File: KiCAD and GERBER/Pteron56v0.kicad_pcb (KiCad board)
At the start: 2 copper layers, 136.1 x 108.1 mm, 46 parts, among them J1 AudioJack4, J2 AudioJack4, SW10 SW_PUSH, SW12 SW_PUSH, SW13 SW_PUSH, SW14 SW_PUSH, SW15 SW_PUSH, SW17 SW_PUSH, SW18 SW_PUSH, SW19 SW_PUSH, SW20 SW_PUSH, SW22 SW_PUSH, SW23 SW_PUSH, SW24 SW_PUSH, SW26 SW_PUSH, SW27 SW_PUSH, SW28 SW_PUSH, SW7 SW_PUSH, SW8 SW_PUSH, SW9 SW_PUSH, U1 ProMicro

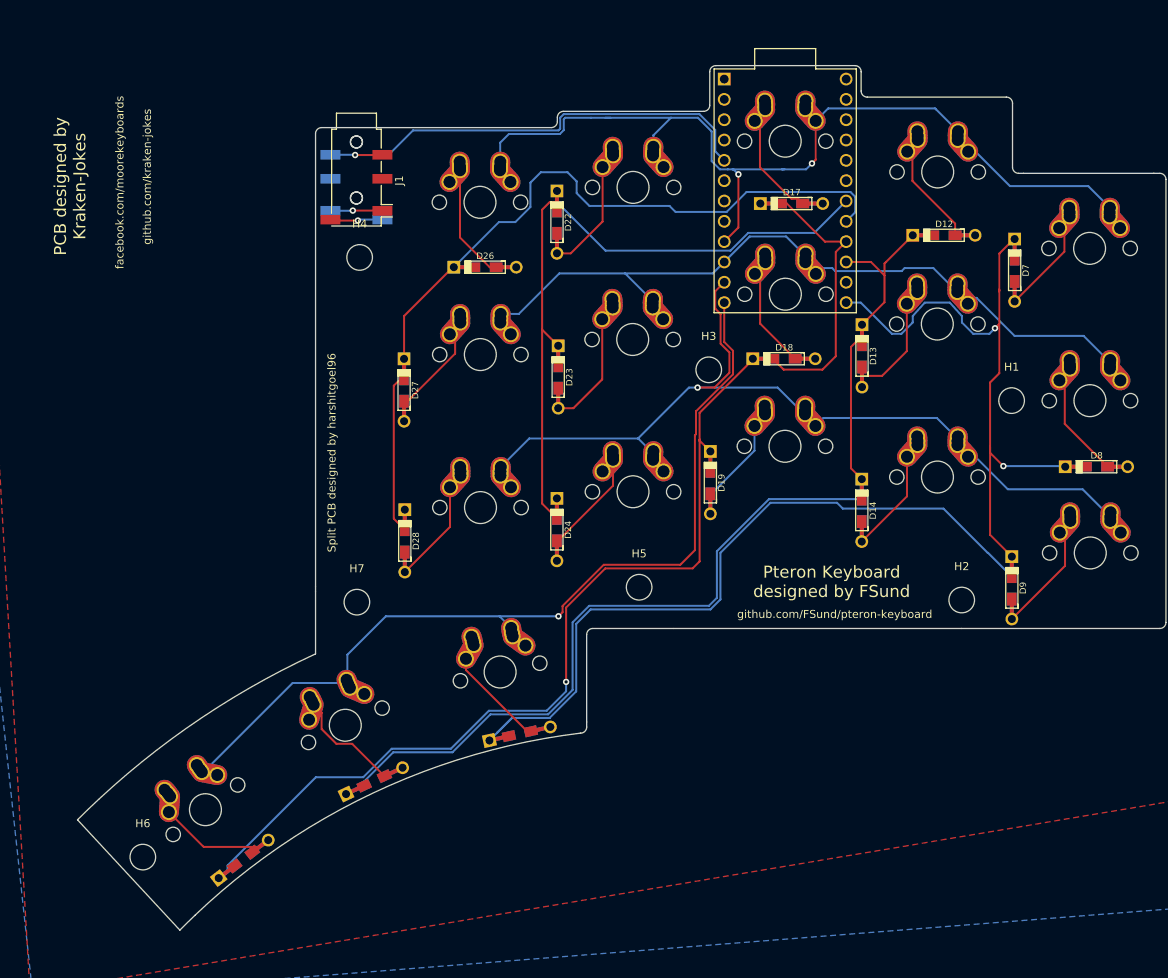
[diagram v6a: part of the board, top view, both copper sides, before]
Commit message: simplified wiring, lily58 like pro micro placement
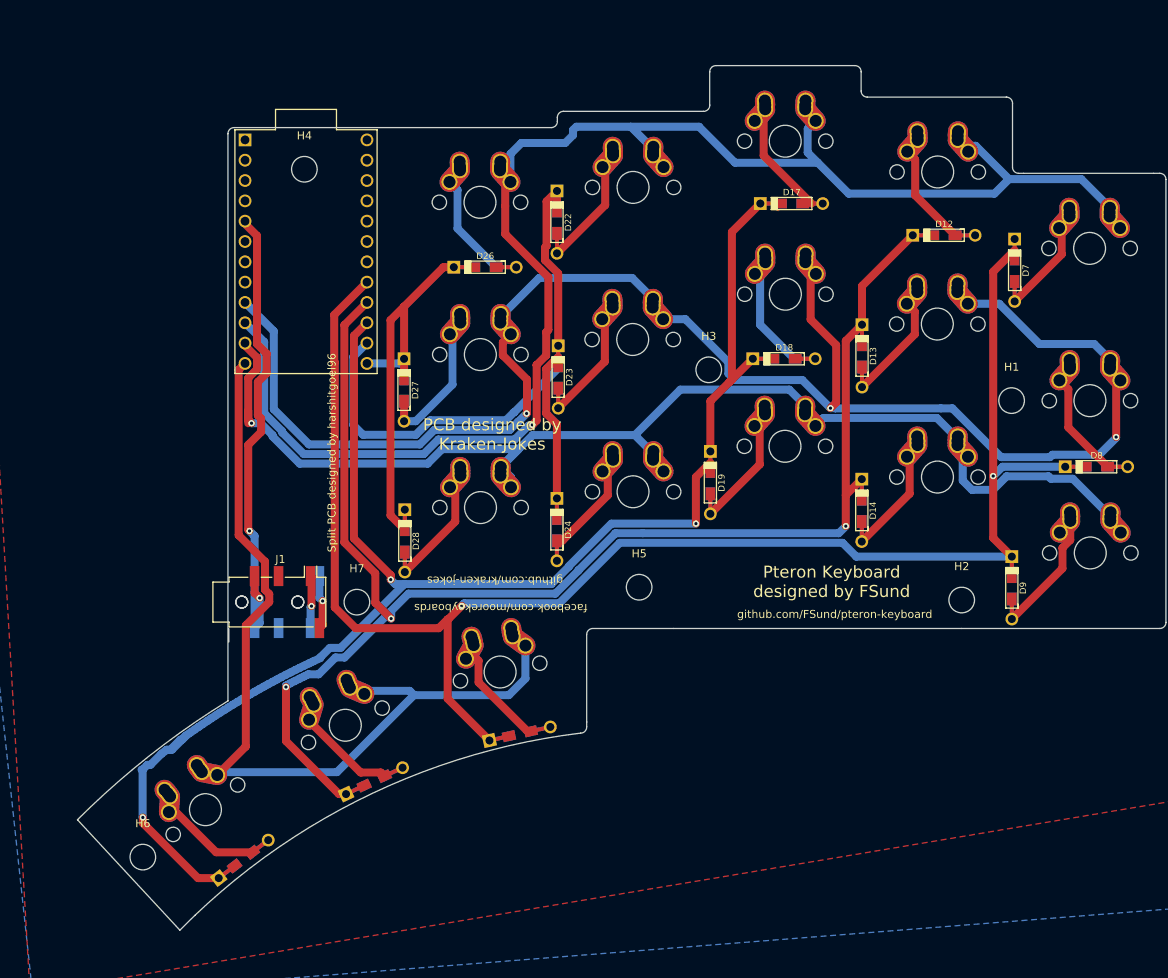
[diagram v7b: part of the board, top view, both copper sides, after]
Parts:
- moved U1 60.4 mm to (99.6, 59.2)
- moved J1 53.6 mm to (96.4, 103.0), turned to 0 degrees
- moved J2 53.6 mm to (96.4, 103.0), turned to 0 degrees
- moved H4 13.0 mm to (99.4, 48.9)
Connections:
- U1 pad 10: /Row2 -> /Row1
- U1 pad 13: /Col1 -> /Col5
- U1 pad 14: (no net) -> /Col4
- U1 pad 15: /Col2 -> /Col3
- U1 pad 16: /Col3 -> /Col2
- U1 pad 17: /Col5 -> /Col1
- U1 pad 18: /Col4 -> (no net)
- U1 pad 9: /Row1 -> /Row2
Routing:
- net /Row2: track 89.7 -> 197.0 mm, vias 0 -> 3
- net /Row1: track 111.2 -> 187.2 mm, vias 2 -> 1
- net /Col2: track 124.9 -> 181.9 mm, vias 0 -> 3
- net /Col5: track 99.8 -> 50.7 mm
- net /Row3: track 105.7 -> 146.8 mm
- net /Col3: track 147.0 -> 186.6 mm, vias 1 -> 3
- net /Col1: track 175.8 -> 200.4 mm
- net Net-(D24-Pad2): track 15.5 -> 12.4 mm
- net /Col4: track 85.7 -> 82.8 mm
- net Net-(D19-Pad2): track 11.9 -> 14.3 mm
- net Net-(D27-Pad2): track 14.2 -> 15.9 mm
- net Net-(D26-Pad2): track 14.5 -> 13.1 mm
- net /Serial: track 59.5 -> 60.6 mm, vias 1 -> 2
- net Net-(D9-Pad2): track 14.3 -> 15.3 mm
- net Net-(D28-Pad2): track 12.9 -> 13.9 mm
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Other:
- outline, holes or cut-outs redrawn

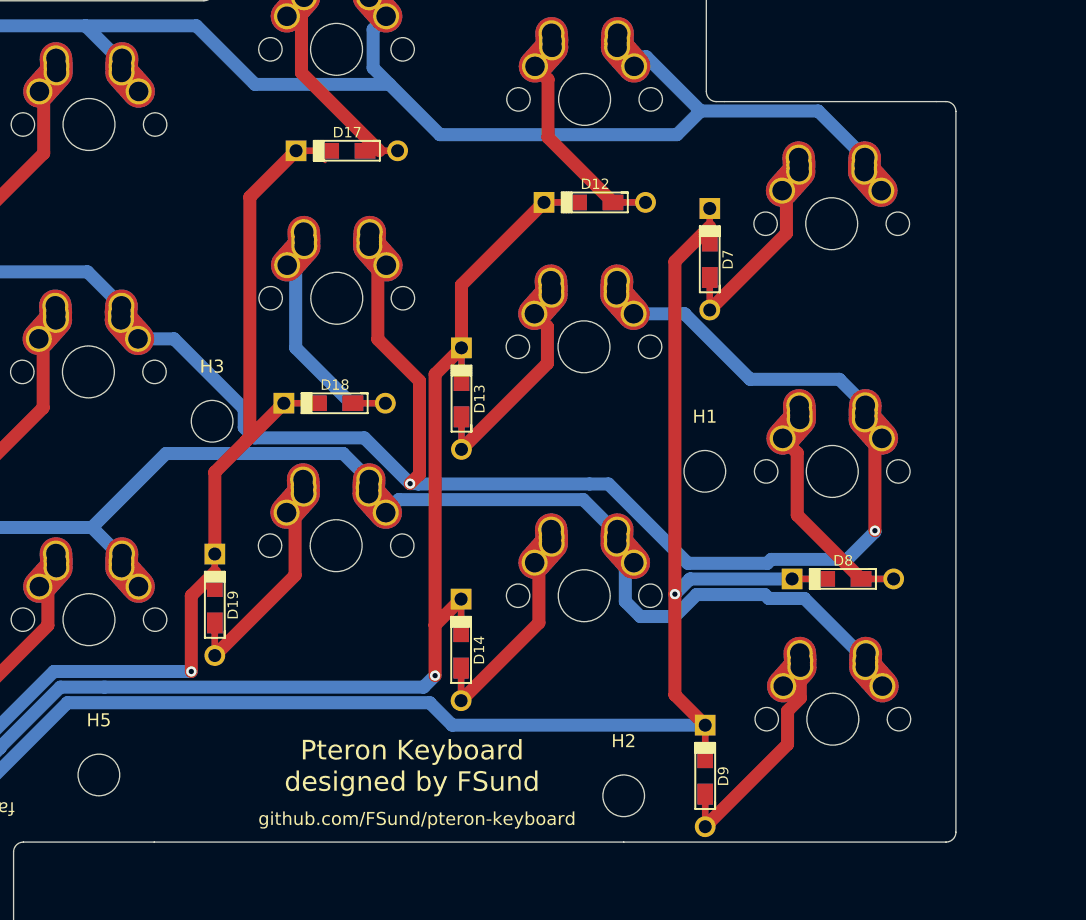
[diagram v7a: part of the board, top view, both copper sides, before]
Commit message: made small changes for mounting holes
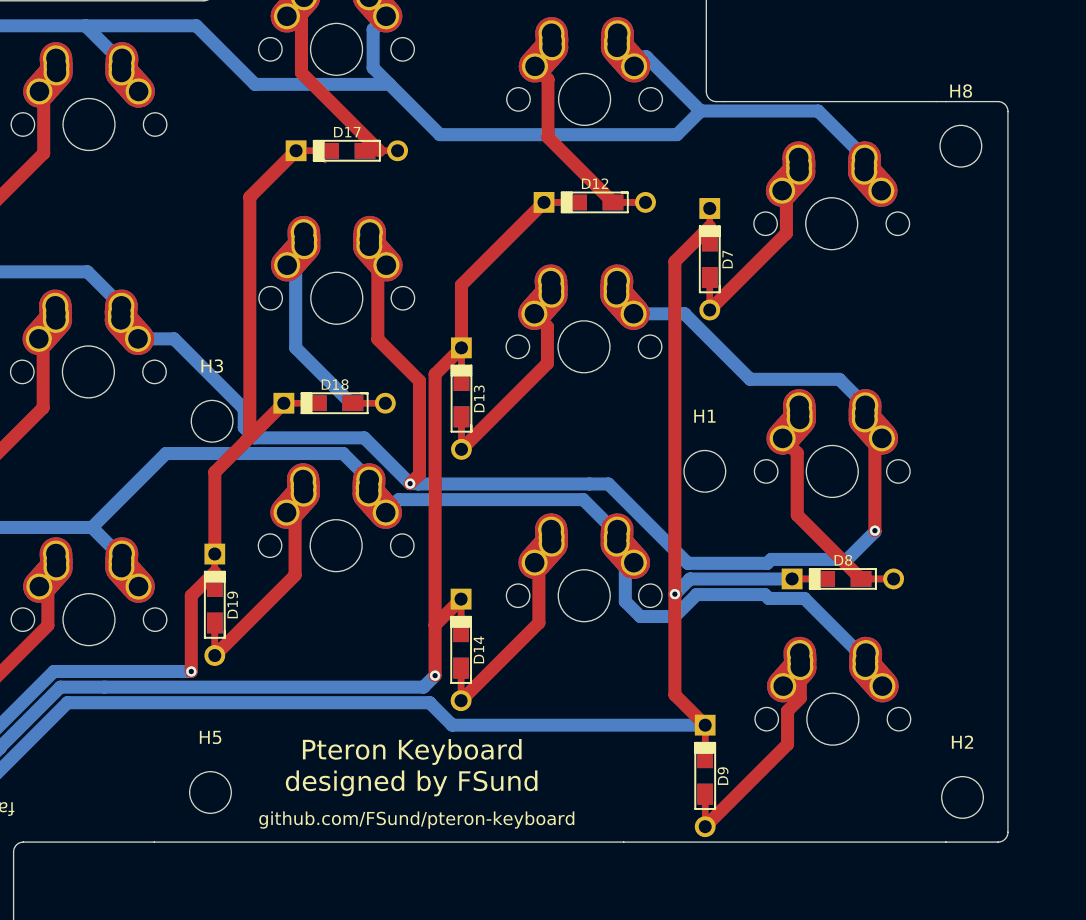
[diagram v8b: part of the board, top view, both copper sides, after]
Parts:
- added H8: MountingHole, MountingHole:MountingHole_3.2mm_M3, F.Cu at (207.5, 52.8)
- moved H2 26.0 mm to (207.6, 102.9)
- moved H5 8.68 mm to (149.9, 102.5)
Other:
- board size 136.1 x 108.1 mm -> 140.1 x 108.1 mm
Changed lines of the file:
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@@
   (general
     (thickness 1.6)
-    (drawings 54)
+    (drawings 56)
     (tracks 400)
     (zones 0)
-    (modules 46)
+    (modules 47)
     (nets 31)
   )
@@
     (39 F.Mask user hide)
     (40 Dwgs.User user)
-    (41 Cmts.User user hide)
+    (41 Cmts.User user)
     (42 Eco1.User user hide)
     (43 Eco2.User user hide)
@@
     (add_net VCC)
   )
+  (module MountingHole:MountingHole_3.2mm_M3 (layer F.Cu)
+    (at 207.518 52.832)
+    (descr "Mounting Hole 3.2mm, no annular, M3")
+    (tags "mounting hole 3.2mm no annular m3")
+    (attr virtual)
+    (fp_text reference H8 (at 0 -4.2) (layer F.SilkS)
+      (effects (font (size 1 1) (thickness 0.15)))
+    )
+    (fp_text value MountingHole (at 0 4.2) (layer F.Fab)
+      (effects (font (size 1 1) (thickness 0.15)))
+    )
+    (fp_text user %R (at 0.3 0) (layer F.Fab)
+      (effects (font (size 1 1) (thickness 0.15)))
+    )
+    (fp_circle (center 0 0) (end 3.2 0) (layer Cmts.User) (width 0.15))
+    (fp_circle (center 0 0) (end 3.45 0) (layer F.CrtYd) (width 0.05))
+    (pad 1 np_thru_hole circle (at 0 0) (size 3.2 3.2) (drill 3.2) (layers *.Cu *.Mask))
+  )
   (module promicro:ProMicro (layer F.Cu)
     (at 99.6442 59.1947 270)
@@
   )
   (module MountingHole:MountingHole_3.2mm_M3 (layer F.Cu)
-    (at 141.2875 101.1428)
+    (at 149.86 102.489)
     (descr "Mounting Hole 3.2mm, no annular, M3")
     (tags "mounting hole 3.2mm no annular m3")
@@
   )
   (module MountingHole:MountingHole_3.2mm_M3 (layer F.Cu)
-    (at 181.61 102.743)
+    (at 207.645 102.87)
     (descr "Mounting Hole 3.2mm, no annular, M3")
     (tags "mounting hole 3.2mm no annular m3")
@@
     )
   )
+  (gr_line (start 206.375 106.299) (end 210.375 106.299) (layer Edge.Cuts) (width 0.05))
+  (gr_line (start 206.375 49.403) (end 210.375 49.403) (layer Edge.Cuts) (width 0.05))
   (gr_line (start 71.076237 130.207471) (end 83.878669 144.009293) (layer Edge.Cuts) (width 0.05))
   (gr_arc (start 144.1069 203.3651) (end 89.889001 115.354101) (angle -13.31569458) (layer Edge.Cuts) (width 0.05))
   (gr_line (start 89.889 44.45) (end 89.889 115.3541) (layer Edge.Cuts) (width 0.05))
   (gr_line (start 90.651 43.688) (end 103.251 43.688) (layer Edge.Cuts) (width 0.05))
-  (gr_line (start 207.137 50.165) (end 207.137 105.537) (layer Edge.Cuts) (width 0.05))
+  (gr_line (start 211.137 50.165) (end 211.137 105.537) (layer Edge.Cuts) (width 0.05))
   (gr_arc (start 144.1704 203.3397) (end 85.763282 142.153111) (angle -1.791806826) (layer Edge.Cuts) (width 0.05))
   (gr_line (start 104.557841 118.39453) (end 146.819667 209.025309) (layer Dwgs.User) (width 0.15))
@@
   (gr_line (start 181.61 106.299) (end 206.375 106.299) (layer Edge.Cuts) (width 0.05))
   (gr_line (start 205.613 49.403) (end 206.375 49.403) (layer Edge.Cuts) (width 0.05))
-  (gr_arc (start 206.375 50.165) (end 207.137 50.165) (angle -90) (layer Edge.Cuts) (width 0.05))
-  (gr_arc (start 206.375 105.537) (end 206.375 106.299) (angle -90) (layer Edge.Cuts) (width 0.05))
+  (gr_arc (start 210.375 50.165) (end 211.137 50.165) (angle -90) (layer Edge.Cuts) (width 0.05))
+  (gr_arc (start 210.375 105.537) (end 210.375 106.299) (angle -90) (layer Edge.Cuts) (width 0.05))
   (gr_line (start 145.542 106.299) (end 181.61 106.299) (layer Edge.Cuts) (width 0.05))
   (gr_line (start 134.73 107.061) (end 134.73 117.983) (layer Edge.Cuts) (width 0.05))
